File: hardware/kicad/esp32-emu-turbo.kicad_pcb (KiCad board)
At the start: 4 copper layers, 160 x 75 mm, 85 parts, among them J1 USB-C-16P, J3 JST-PH-2P-SMD, J4 FPC-40P-0.5mm, SW1 SW-SMD-5.1x5.1, SW10 SW-SMD-5.1x5.1, SW11 SW-SMD-5.1x5.1, SW12 SW-SMD-5.1x5.1, SW13 SW-SMD-5.1x5.1, SW2 SW-SMD-5.1x5.1, SW3 SW-SMD-5.1x5.1, SW4 SW-SMD-5.1x5.1, SW5 SW-SMD-5.1x5.1, SW6 SW-SMD-5.1x5.1, SW7 SW-SMD-5.1x5.1, SW8 SW-SMD-5.1x5.1, SW9 SW-SMD-5.1x5.1, U1 ESP32-S3-WROOM-1-N16R8, U2 ESOP-8, U3 SOT-223, U5 SOP-16, U6 TF-01A

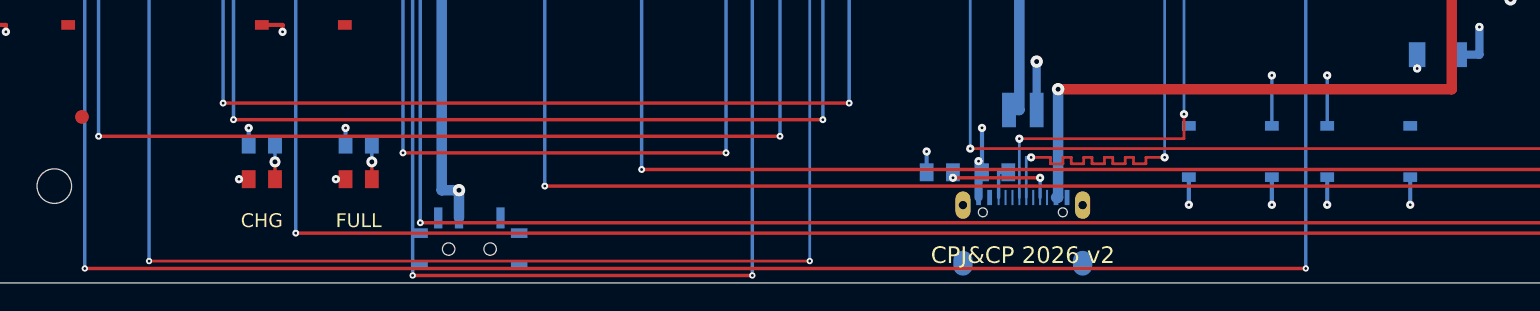
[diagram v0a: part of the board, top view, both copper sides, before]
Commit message: feat(pcb): USB-C shield THT + extra GND/VBUS pads + BTN_START bypass
- Rear shield pads 13b/14b changed from SMD to THT (0.6mm drill per datasheet)
- All 4 shield pads (13, 14, 13b, 14b) now assigned to GND net for EMI/ESD
- USB-C pad 1 connected to GND (extra return path)
- USB-C pads 9, 11 connected to VBUS (3A current support)
- VBUS B.Cu vertical shifted x=82.55→82.45 for GND pad 1 clearance
- BTN_START F.Cu trace bypasses rear shield THT pads via north jog (y=72.38)
- All 115 DFM + 9 DFA + 25 JLCPCB tests pass

Co-Authored-By: Claude Opus 4.6 (1M context) <noreply@anthropic.com>
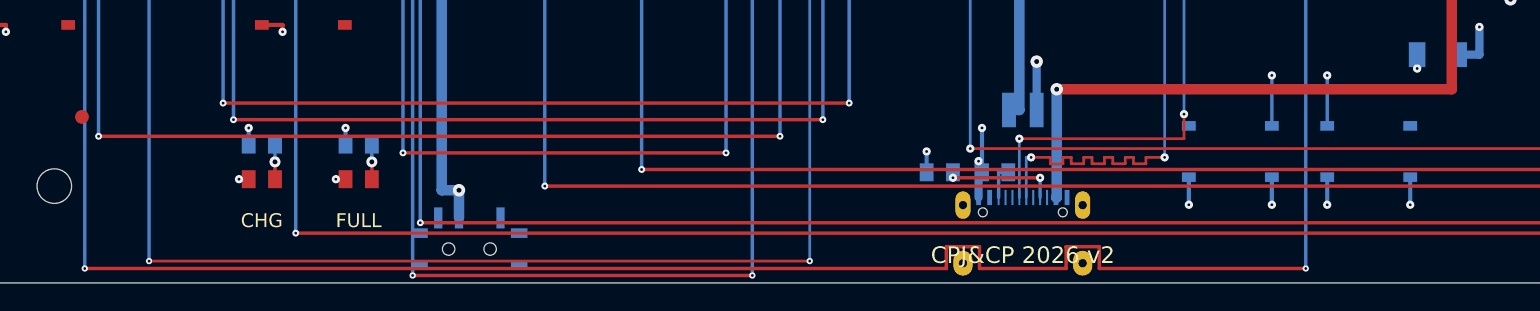
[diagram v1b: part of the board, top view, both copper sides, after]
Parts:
- removed the C25 at (31.5, 37.5)
- removed the L1 at (110.0, 52.5)
- removed the SW10 at (28.0, 54.5)
- added FID1: Fiducial, Fiducial, F.Cu at (12.0, 12.0)
- added LED1: LED_0805, LED_0805, F.Cu at (25.0, 67.5)
- added R1: R_0805, R_0805, B.Cu at (74.0, 67.0)
- C25: renamed from FID1; value Fiducial -> C_0805; footprint Fiducial -> C_0805; moved to B.Cu
- L1: renamed from SW_RST; value SW-SMD-5.1x5.1 -> SMD-4x4x2; footprint SW-SMD-5.1x5.1 -> SMD-4x4x2
- SW10: renamed from LED1; value LED_0805 -> SW-SMD-5.1x5.1; footprint LED_0805 -> SW-SMD-5.1x5.1
- SW_RST: renamed from R1; value R_0805 -> SW-SMD-5.1x5.1; footprint R_0805 -> SW-SMD-5.1x5.1
- moved C25 32.1 mm to (31.5, 37.5)
- moved SW_RST 21.1 mm to (95.0, 65.5)
- moved L1 19.8 mm to (110.0, 52.5)
- moved SW10 13.3 mm to (28.0, 54.5)
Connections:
- C25 pad 1: (no net) -> +5V
- J1 pad 1: (no net) -> GND
- J1 pad 11: (no net) -> VBUS
- J1 pad 13: (no net) -> GND
- J1 pad 13b: (no net) -> GND
- J1 pad 14: (no net) -> GND
- J1 pad 14b: (no net) -> GND
- J1 pad 9: (no net) -> VBUS
- L1 pad 1: EN -> BAT+
- L1 pad 2: (no net) -> LX
- SW10 pad 1: GND -> (no net)
- SW10 pad 2: LED1_RA -> BTN_SELECT
- SW_RST pad 1: USB_CC1 -> EN
- SW_RST pad 2: GND -> (no net)
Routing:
- net BTN_START: track 165.5 -> 171.8 mm
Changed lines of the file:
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@@
     (property "Reference" "J1" (at 0 -6 0) (layer "B.Fab") (effects (font (size 1 1) (thickness 0.2)) (justify mirror)))
     (property "Value" "USB-C-16P" (at 0 4 0) (layer "B.Fab") (effects (font (size 1 1) (thickness 0.2)) (justify mirror)))
-    (pad "1" smd rect (at 3.2 -2.375) (size 0.35 1.1) (layers "B.Cu" "B.Paste" "B.Mask") (net 0 "") (solder_mask_margin 0))
+    (pad "1" smd rect (at 3.2 -2.375) (size 0.35 1.1) (layers "B.Cu" "B.Paste" "B.Mask") (net 1 "GND") (solder_mask_margin 0))
     (pad "2" smd rect (at 2.4 -2.375) (size 0.35 1.1) (layers "B.Cu" "B.Paste" "B.Mask") (net 2 "VBUS") (solder_mask_margin 0))
-    (pad "11" smd rect (at -2.4 -2.375) (size 0.35 1.1) (layers "B.Cu" "B.Paste" "B.Mask") (net 0 "") (solder_mask_margin 0))
+    (pad "11" smd rect (at -2.4 -2.375) (size 0.35 1.1) (layers "B.Cu" "B.Paste" "B.Mask") (net 2 "VBUS") (solder_mask_margin 0))
     (pad "12" smd rect (at -3.2 -2.375) (size 0.35 1.1) (layers "B.Cu" "B.Paste" "B.Mask") (net 1 "GND") (solder_mask_margin 0))
     (pad "3" smd rect (at 1.75 -2.375) (size 0.15 1.1) (layers "B.Cu" "B.Paste" "B.Mask") (net 0 "") (solder_mask_margin 0))
@@
     (pad "7" smd rect (at -0.25 -2.375) (size 0.15 1.1) (layers "B.Cu" "B.Paste" "B.Mask") (net 41 "USB_D-") (solder_mask_margin 0))
     (pad "8" smd rect (at -0.75 -2.375) (size 0.15 1.1) (layers "B.Cu" "B.Paste" "B.Mask") (net 0 "") (solder_mask_margin 0))
-    (pad "9" smd rect (at -1.25 -2.375) (size 0.15 1.1) (layers "B.Cu" "B.Paste" "B.Mask") (net 0 "") (solder_mask_margin 0))
+    (pad "9" smd rect (at -1.25 -2.375) (size 0.15 1.1) (layers "B.Cu" "B.Paste" "B.Mask") (net 2 "VBUS") (solder_mask_margin 0))
     (pad "10" smd rect (at -1.75 -2.375) (size 0.15 1.1) (layers "B.Cu" "B.Paste" "B.Mask") (net 49 "USB_CC2") (solder_mask_margin 0))
-    (pad "13" thru_hole oval (at 4.325 -1.825) (size 1.1 2.0) (drill 0.6) (layers "*.Cu" "*.Mask") (net 0 "") (solder_mask_margin 0))
-    (pad "14" thru_hole oval (at -4.325 -1.825) (size 1.1 2.0) (drill 0.6) (layers "*.Cu" "*.Mask") (net 0 "") (solder_mask_margin 0))
-    (pad "13b" smd oval (at 4.325 2.375) (size 1.4 1.8) (layers "B.Cu" "B.Paste" "B.Mask") (net 0 "") (solder_mask_margin 0))
-    (pad "14b" smd oval (at -4.325 2.375) (size 1.4 1.8) (layers "B.Cu" "B.Paste" "B.Mask") (net 0 "") (solder_mask_margin 0))
+    (pad "13" thru_hole oval (at 4.325 -1.825) (size 1.1 2.0) (drill 0.6) (layers "*.Cu" "*.Mask") (net 1 "GND") (solder_mask_margin 0))
+    (pad "14" thru_hole oval (at -4.325 -1.825) (size 1.1 2.0) (drill 0.6) (layers "*.Cu" "*.Mask") (net 1 "GND") (solder_mask_margin 0))
+    (pad "13b" thru_hole oval (at 4.325 2.375) (size 1.4 1.8) (drill 0.6) (layers "*.Cu" "*.Mask") (net 1 "GND") (solder_mask_margin 0))
+    (pad "14b" thru_hole oval (at -4.325 2.375) (size 1.4 1.8) (drill 0.6) (layers "*.Cu" "*.Mask") (net 1 "GND") (solder_mask_margin 0))
     (pad "" np_thru_hole circle (at 2.89 -1.305) (size 0.65 0.65) (drill 0.65) (layers "*.Cu" "*.Mask"))
     (pad "" np_thru_hole circle (at -2.89 -1.305) (size 0.65 0.65) (drill 0.65) (layers "*.Cu" "*.Mask"))
@@
     (pad "1" smd circle (at 0 0) (size 1.0 1.0) (layers "F.Cu" "F.Mask") (net 0 "") (solder_mask_margin 0.5))
   )
-  (segment (start 82.4 68.825) (end 82.55000000000001 68.825) (width 0.76) (layer "B.Cu") (net 2))
-  (segment (start 82.55000000000001 68.825) (end 82.55000000000001 61.0) (width 0.76) (layer "B.Cu") (net 2))
-  (via (at 82.55000000000001 61.0) (size 0.9) (drill 0.35) (layers "F.Cu" "B.Cu") (net 2))
-  (segment (start 82.55000000000001 61.0) (end 111.0 61.0) (width 0.76) (layer "F.Cu") (net 2))
+  (segment (start 82.4 68.825) (end 82.45 68.825) (width 0.76) (layer "B.Cu") (net 2))
+  (segment (start 82.45 68.825) (end 82.45 61.0) (width 0.76) (layer "B.Cu") (net 2))
+  (via (at 82.45 61.0) (size 0.9) (drill 0.35) (layers "F.Cu" "B.Cu") (net 2))
+  (segment (start 82.45 61.0) (end 111.0 61.0) (width 0.76) (layer "F.Cu") (net 2))
   (segment (start 111.0 61.0) (end 111.0 40.095) (width 0.76) (layer "F.Cu") (net 2))
   (via (at 111.0 40.095) (size 0.9) (drill 0.35) (layers "F.Cu" "B.Cu") (net 2))
@@
   (segment (start 12.2 52.65) (end 12.2 73.955) (width 0.25) (layer "B.Cu") (net 35))
   (via (at 12.2 73.955) (size 0.46) (drill 0.2) (layers "F.Cu" "B.Cu") (net 35))
-  (segment (start 12.2 73.955) (end 100.45 73.955) (width 0.25) (layer "F.Cu") (net 35))
+  (segment (start 12.2 73.955) (end 74.47 73.955) (width 0.25) (layer "F.Cu") (net 35))
+  (segment (start 74.47 73.955) (end 74.47 72.38) (width 0.25) (layer "F.Cu") (net 35))
+  (segment (start 74.47 72.38) (end 76.87 72.38) (width 0.25) (layer "F.Cu") (net 35))
+  (segment (start 76.87 72.38) (end 76.87 73.955) (width 0.25) (layer "F.Cu") (net 35))
+  (segment (start 76.87 73.955) (end 83.13 73.955) (width 0.25) (layer "F.Cu") (net 35))
+  (segment (start 83.13 73.955) (end 83.13 72.38) (width 0.25) (layer "F.Cu") (net 35))
+  (segment (start 83.13 72.38) (end 85.53 72.38) (width 0.25) (layer "F.Cu") (net 35))
+  (segment (start 85.53 72.38) (end 85.53 73.955) (width 0.25) (layer "F.Cu") (net 35))
+  (segment (start 85.53 73.955) (end 100.45 73.955) (width 0.25) (layer "F.Cu") (net 35))
   (via (at 100.45 73.955) (size 0.46) (drill 0.2) (layers "F.Cu" "B.Cu") (net 35))
   (segment (start 100.45 73.955) (end 100.45 34.94) (width 0.25) (layer "B.Cu") (net 35))

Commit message: feat(pcb): add USB ESD protection (USBLC6-2SC6 TVS + 22Ω series resistors)
Add USBLC6-2SC6 TVS diode (U4, SOT-23-6) and 2x 22Ω 0402 series
resistors (R22/R23) on USB D+/D- lines for ±8kV ESD protection.

Components:
- U4 at (90.95, 60.0): TVS pins overlap D+/D- approach columns
- R22 at (90.25, 40.0): 22Ω inline on D+ B.Cu vertical
- R23 at (91.65, 38.5): 22Ω inline on D- B.Cu vertical
- New nets: USB_DP_MCU, USB_DM_MCU (ESP32 side after resistors)

Verification: 115/115 DFM, 9/9 DFA, 47/47 polarity, 60/60 review,
25/25 JLCPCB, 3/3 ESD protection — all pass.

Co-Authored-By: Claude Opus 4.6 (1M context) <noreply@anthropic.com>
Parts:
- removed the C13 at (83.0, 50.0)
- removed the J1 at (80.0, 71.2)
- removed the J3 at (80.0, 62.5)
- removed the L1 at (110.0, 52.5)
- removed the SW1 at (18.0, 23.5)
- removed the SW2 at (18.0, 41.5)
- removed the SW3 at (9.00, 32.5)
- removed the U5 at (30.0, 29.5)
- added FID1: Fiducial, Fiducial, F.Cu at (12.0, 12.0)
- added R18: R_0805, R_0805, B.Cu at (32.0, 65.0)
- added R22: R_0402, R_0402, B.Cu at (90.2, 40.0)
- added R23: R_0402, R_0402, B.Cu at (91.7, 38.5)
- added R4: R_0805, R_0805, B.Cu at (43.0, 46.0)
- added R5: R_0805, R_0805, B.Cu at (48.0, 46.0)
- added SW10: SW-SMD-5.1x5.1, SW-SMD-5.1x5.1, F.Cu at (28.0, 54.5)
- added SW13: SW-SMD-5.1x5.1, SW-SMD-5.1x5.1, F.Cu at (142.0, 61.7)
- added SW9: SW-SMD-5.1x5.1, SW-SMD-5.1x5.1, F.Cu at (8.00, 54.5)
- added U2: ESOP-8, ESOP-8, B.Cu at (110.0, 42.5)
- added U4: SOT-23-6, SOT-23-6, B.Cu at (91.0, 60.0)
- C13: renamed from FID1; value Fiducial -> C_0805; footprint Fiducial -> C_0805; moved to B.Cu
- J1: renamed from U2; value ESOP-8 -> USB-C-16P; footprint ESOP-8 -> USB-C-16P
- J3: renamed from R5; value R_0805 -> JST-PH-2P-SMD; footprint R_0805 -> JST-PH-2P-SMD
- L1: renamed from R4; value R_0805 -> SMD-4x4x2; footprint R_0805 -> SMD-4x4x2
- U5: renamed from R18; value R_0805 -> SOP-16; footprint R_0805 -> SOP-16
- moved SW3 136.2 mm to (9.00, 32.5)
- moved C13 80.5 mm to (83.0, 50.0)
- moved L1 67.3 mm to (110.0, 52.5)
- moved J1 41.5 mm to (80.0, 71.2)
- moved J3 36.0 mm to (80.0, 62.5)
- moved U5 35.6 mm to (30.0, 29.5)
- moved SW1 32.6 mm to (18.0, 23.5)
- moved SW2 16.4 mm to (18.0, 41.5)
- renumbered SW9 to SW1, SW10 to SW2, SW13 to SW3
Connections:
- J1 pad 1: VBUS -> GND
- J1 pad 2: (no net) -> VBUS
- J1 pad 4: (no net) -> USB_CC1
- J1 pad 5: IP5306_KEY -> (no net)
- J1 pad 6: BAT+ -> USB_D+
- J1 pad 7: LX -> USB_D-
- J1 pad 8: +5V -> (no net)
- J3 pad 1: (no net) -> BAT+
- J3 pad 2: (no net) -> GND
- L1 pad 1: (no net) -> BAT+
- L1 pad 2: (no net) -> LX
- SW1 pad 2: BTN_START -> BTN_UP
- SW2 pad 2: BTN_SELECT -> BTN_DOWN
- SW3 pad 2: (no net) -> BTN_LEFT
- SW3 pad 3: (no net) -> GND
- U1 pad 13: USB_D- -> USB_DM_MCU
- U1 pad 14: USB_D+ -> USB_DP_MCU
- U5 pad 1: LED2_RA -> (no net)
- U5 pad 2: +3V3 -> GND
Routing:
- net USB_D-: track 46.5 -> 42.1 mm
- net USB_DM_MCU: track 0.00 -> 3.44 mm
- net USB_D+: track 46.2 -> 42.9 mm
- net USB_DP_MCU: track 0.00 -> 2.27 mm
- net VBUS: track 61.2 -> 63.3 mm, vias 3 -> 4
- net GND: track 170.7 -> 171.5 mm, vias 77 -> 78
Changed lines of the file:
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@@
   (net 52 "LED2_RA")
   (net 53 "EN")
+  (net 54 "USB_DP_MCU")
+  (net 55 "USB_DM_MCU")
   (gr_line (start 6.0 0) (end 154.0 0) (stroke (width 0.05) (type default)) (layer "Edge.Cuts"))
   (gr_line (start 160.0 6.0) (end 160.0 69.0) (stroke (width 0.05) (type default)) (layer "Edge.Cuts"))
@@
     (pad "11" smd rect (at 8.75 7.4399999999999995) (size 1.5 0.9) (layers "B.Cu" "B.Paste" "B.Mask") (net 35 "BTN_START"))
     (pad "12" smd rect (at 8.75 8.71) (size 1.5 0.9) (layers "B.Cu" "B.Paste" "B.Mask") (net 10 "LCD_D4"))
-    (pad "13" smd rect (at 8.75 9.98) (size 1.5 0.9) (layers "B.Cu" "B.Paste" "B.Mask") (net 41 "USB_D-"))
-    (pad "14" smd rect (at 8.75 11.250000000000002) (size 1.5 0.9) (layers "B.Cu" "B.Paste" "B.Mask") (net 40 "USB_D+"))
+    (pad "13" smd rect (at 8.75 9.98) (size 1.5 0.9) (layers "B.Cu" "B.Paste" "B.Mask") (net 55 "USB_DM_MCU"))
+    (pad "14" smd rect (at 8.75 11.250000000000002) (size 1.5 0.9) (layers "B.Cu" "B.Paste" "B.Mask") (net 54 "USB_DP_MCU"))
     (pad "15" smd rect (at 6.985 12.5) (size 0.9 1.5) (layers "B.Cu" "B.Paste" "B.Mask") (net 38 "BTN_R"))
     (pad "16" smd rect (at 5.715 12.5) (size 0.9 1.5) (layers "B.Cu" "B.Paste" "B.Mask") (net 17 "LCD_WR"))
@@
     (pad "1" smd rect (at 0.95 0) (size 1.0 1.3) (layers "B.Cu" "B.Paste" "B.Mask") (net 49 "USB_CC2"))
     (pad "2" smd rect (at -0.95 0) (size 1.0 1.3) (layers "B.Cu" "B.Paste" "B.Mask") (net 1 "GND"))
+  )
+  (footprint "SOT-23-6" (at 90.95 60.0) (layer "B.Cu")
+    (property "Reference" "U4" (at 0 -3 0) (layer "B.Fab") (effects (font (size 1 1) (thickness 0.2)) (justify mirror)))
+    (property "Value" "SOT-23-6" (at 0 3 0) (layer "B.Fab") (effects (font (size 1 1) (thickness 0.2)) (justify mirror)))
+    (pad "1" smd rect (at 0.95 1.1) (size 0.6 0.7) (layers "B.Cu" "B.Paste" "B.Mask") (net 41 "USB_D-"))
+    (pad "2" smd rect (at 0.0 1.1) (size 0.6 0.7) (layers "B.Cu" "B.Paste" "B.Mask") (net 1 "GND"))
+    (pad "3" smd rect (at -0.95 1.1) (size 0.6 0.7) (layers "B.Cu" "B.Paste" "B.Mask") (net 40 "USB_D+"))
+    (pad "4" smd rect (at -0.95 -1.1) (size 0.6 0.7) (layers "B.Cu" "B.Paste" "B.Mask") (net 40 "USB_D+"))
+    (pad "5" smd rect (at 0.0 -1.1) (size 0.6 0.7) (layers "B.Cu" "B.Paste" "B.Mask") (net 2 "VBUS"))
+    (pad "6" smd rect (at 0.95 -1.1) (size 0.6 0.7) (layers "B.Cu" "B.Paste" "B.Mask") (net 41 "USB_D-"))
+  )
+  (footprint "R_0402" (at 90.25 40.0) (layer "B.Cu")
+    (property "Reference" "R22" (at 0 -3 0) (layer "B.Fab") (effects (font (size 1 1) (thickness 0.2)) (justify mirror)))
+    (property "Value" "R_0402" (at 0 3 0) (layer "B.Fab") (effects (font (size 1 1) (thickness 0.2)) (justify mirror)))
+    (pad "1" smd rect (at 0.0 -0.48) (size 0.62 0.56) (layers "B.Cu" "B.Paste" "B.Mask") (net 54 "USB_DP_MCU"))
+    (pad "2" smd rect (at 0.0 0.48) (size 0.62 0.56) (layers "B.Cu" "B.Paste" "B.Mask") (net 40 "USB_D+"))
+  )
+  (footprint "R_0402" (at 91.65 38.5) (layer "B.Cu")
+    (property "Reference" "R23" (at 0 -3 0) (layer "B.Fab") (effects (font (size 1 1) (thickness 0.2)) (justify mirror)))
+    (property "Value" "R_0402" (at 0 3 0) (layer "B.Fab") (effects (font (size 1 1) (thickness 0.2)) (justify mirror)))
+    (pad "1" smd rect (at 0.0 -0.48) (size 0.62 0.56) (layers "B.Cu" "B.Paste" "B.Mask") (net 55 "USB_DM_MCU"))
+    (pad "2" smd rect (at 0.0 0.48) (size 0.62 0.56) (layers "B.Cu" "B.Paste" "B.Mask") (net 41 "USB_D-"))
   )
   (footprint "R_0805" (at 65 42) (layer "B.Cu")
@@
   (segment (start 88.9 65.925) (end 90.25 65.925) (width 0.2) (layer "F.Cu") (net 40))
   (via (at 90.25 65.925) (size 0.6) (drill 0.2) (layers "F.Cu" "B.Cu") (net 40))
-  (segment (start 90.25 65.925) (end 90.25 38.75) (width 0.2) (layer "B.Cu") (net 40))
-  (segment (start 90.25 38.75) (end 88.75 38.75) (width 0.2) (layer "B.Cu") (net 40))
+  (segment (start 90.25 65.925) (end 90.25 40.48) (width 0.2) (layer "B.Cu") (net 40))
+  (segment (start 90.25 39.52) (end 90.25 38.75) (width 0.2) (layer "B.Cu") (net 54))
+  (segment (start 90.25 38.75) (end 88.75 38.75) (width 0.2) (layer "B.Cu") (net 54))
   (segment (start 79.75 68.825) (end 79.75 64.575) (width 0.2) (layer "B.Cu") (net 41))
   (via (at 79.75 64.575) (size 0.6) (drill 0.2) (layers "F.Cu" "B.Cu") (net 41))
@@
   (segment (start 91.85000000000001 43.0) (end 91.85000000000001 41.0) (width 0.2) (layer "B.Cu") (net 41))
   (segment (start 91.85000000000001 41.0) (end 91.65 41.0) (width 0.2) (layer "B.Cu") (net 41))
-  (segment (start 91.65 41.0) (end 91.65 37.480000000000004) (width 0.2) (layer "B.Cu") (net 41))
-  (segment (start 91.65 37.480000000000004) (end 88.75 37.480000000000004) (width 0.2) (layer "B.Cu") (net 41))
+  (segment (start 91.65 41.0) (end 91.65 38.98) (width 0.2) (layer "B.Cu") (net 41))
+  (segment (start 91.65 38.02) (end 91.65 37.480000000000004) (width 0.2) (layer "B.Cu") (net 55))
+  (segment (start 91.65 37.480000000000004) (end 88.75 37.480000000000004) (width 0.2) (layer "B.Cu") (net 55))
+  (segment (start 90.95 61.1) (end 90.95 61.9) (width 0.25) (layer "B.Cu") (net 1))
+  (via (at 90.95 61.9) (size 0.6) (drill 0.2) (layers "F.Cu" "B.Cu") (net 1))
+  (segment (start 90.95 58.9) (end 90.95 59.3) (width 0.6) (layer "B.Cu") (net 2))
+  (via (at 90.95 59.3) (size 0.6) (drill 0.2) (layers "F.Cu" "B.Cu") (net 2))
+  (segment (start 90.95 59.3) (end 90.95 61.0) (width 0.6) (layer "F.Cu") (net 2))
   (segment (start 81.25 68.825) (end 81.25 67.4) (width 0.25) (layer "B.Cu") (net 48))
   (via (at 81.25 67.4) (size 0.6) (drill 0.2) (layers "F.Cu" "B.Cu") (net 48))

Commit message: fix(pcb): assign PAM_VREF net to U5 pad 8 (was unconnected)
VREF trace starts offset from pad center to avoid I2S_DOUT collision,
so auto-detection missed it. Explicit _PAD_NETS assignment fixes it.

Co-Authored-By: Claude Opus 4.6 (1M context) <noreply@anthropic.com>
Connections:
- U5 pad 8: (no net) -> PAM_VREF
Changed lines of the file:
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@@
     (pad "6" smd rect (at 1.905 -2.7) (size 0.6 1.55) (layers "B.Cu" "B.Paste" "B.Mask") (net 3 "+5V"))
     (pad "7" smd rect (at 3.175 -2.7) (size 0.6 1.55) (layers "B.Cu" "B.Paste" "B.Mask") (net 26 "I2S_DOUT"))
-    (pad "8" smd rect (at 4.445 -2.7) (size 0.6 1.55) (layers "B.Cu" "B.Paste" "B.Mask") (net 0 ""))
+    (pad "8" smd rect (at 4.445 -2.7) (size 0.6 1.55) (layers "B.Cu" "B.Paste" "B.Mask") (net 50 "PAM_VREF"))
     (pad "9" smd rect (at 4.445 2.7) (size 0.6 1.55) (layers "B.Cu" "B.Paste" "B.Mask") (net 0 ""))
     (pad "10" smd rect (at 3.175 2.7) (size 0.6 1.55) (layers "B.Cu" "B.Paste" "B.Mask") (net 26 "I2S_DOUT"))
